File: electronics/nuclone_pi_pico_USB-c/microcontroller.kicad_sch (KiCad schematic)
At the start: 3 parts, among them J5 Conn_02x06_Odd_Even, U3 RaspberryPiPico

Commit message: prepping for production, updated footprint and versionnumber
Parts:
- U3: footprint SquantorModules:RaspberryPi_Pico_Original_SMD_nokeepout -> SquantorModules:RaspberryPi_Pico_Original_SMD_nokeepout_USB_TP_TH
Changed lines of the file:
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@@
       (effects (font (size 1.27 1.27)))
     )
-    (property "Footprint" "SquantorModules:RaspberryPi_Pico_Original_SMD_nokeepout" (at 81.28 88.9 0)
+    (property "Footprint" "SquantorModules:RaspberryPi_Pico_Original_SMD_nokeepout_USB_TP_TH" (at 81.28 88.9 0)
       (effects (font (size 1.27 1.27)) hide)
     )

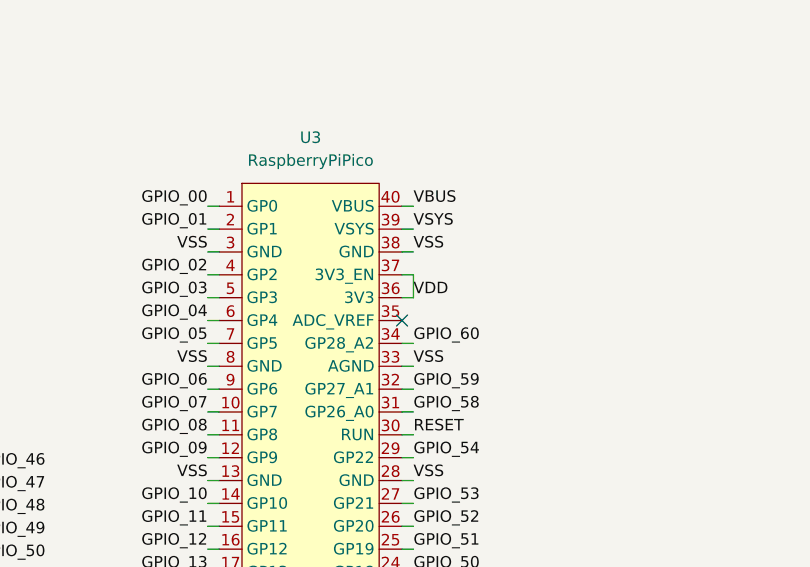
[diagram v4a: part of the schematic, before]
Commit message: fixed error with EN pin of raspberry pi pico, respin required
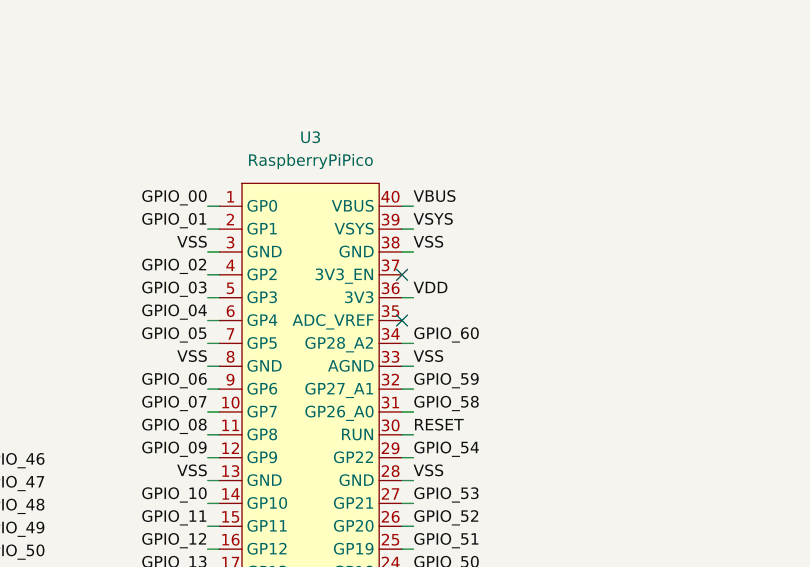
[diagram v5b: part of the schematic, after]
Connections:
- net VDD: no longer U3.37 (3V3_EN)
- no-connect marks 38 -> 39
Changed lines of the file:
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@@
   (no_connect (at 43.18 58.42))
   (no_connect (at 24.13 116.84))
+  (no_connect (at 91.44 72.39))
   (no_connect (at 43.18 66.04))
   (no_connect (at 24.13 106.68))
@@
     (stroke (width 0) (type default))
   )
-  (wire (pts (xy 91.44 72.39) (xy 92.71 72.39))
-    (stroke (width 0) (type default))
-  )
   (wire (pts (xy 24.13 55.88) (xy 25.4 55.88))
     (stroke (width 0) (type default))
@@
     (stroke (width 0) (type default))
   )
-  (wire (pts (xy 92.71 72.39) (xy 92.71 74.93))
-    (stroke (width 0) (type default))
-  )
